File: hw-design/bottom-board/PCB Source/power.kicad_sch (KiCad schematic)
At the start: 29 parts, among them J1 Power Jack, J2 HMI_POWER, U1 TL750M10CKVURG3, U15 LM2596S-5, U2 LD1117S50TR

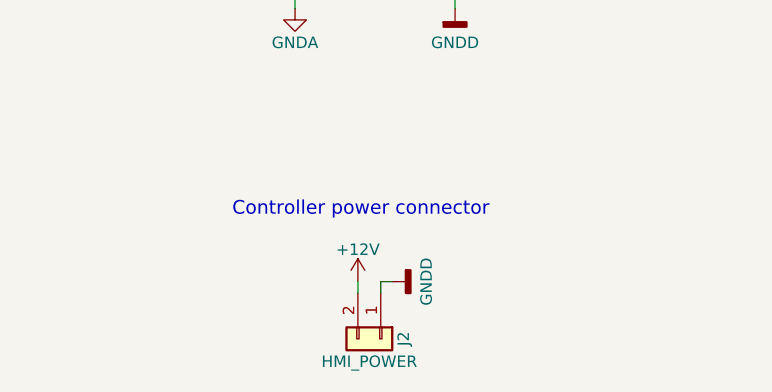
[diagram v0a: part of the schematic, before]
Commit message: change HMI connector type
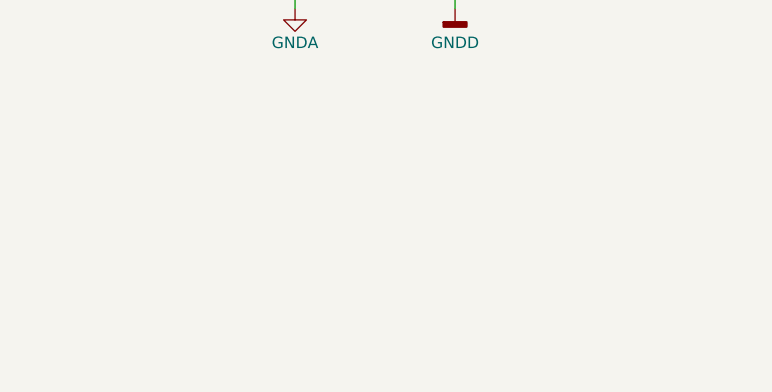
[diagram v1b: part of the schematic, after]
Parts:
- removed J2: HMI_POWER, footprints:B2B-XH-A, symbol bottom-board-rescue:Conn_01x02-Connector_Generic
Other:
- note removed: "Controller power connector"
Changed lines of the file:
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@@
-    (stroke (width 0) (type default) (color 0 0 0 0))
-  )
-  (wire (pts (xy 239.903 148.463) (xy 239.903 147.193))
     (stroke (width 0) (type default) (color 0 0 0 0))
   )
@@
     (stroke (width 0) (type default) (color 0 0 0 0))
   )
-  (wire (pts (xy 239.903 147.193) (xy 241.173 147.193))
-    (stroke (width 0) (type default) (color 0 0 0 0))
-  )
   (wire (pts (xy 195.072 99.06) (xy 195.072 93.98))
     (stroke (width 0) (type default) (color 0 0 0 0))
@@
   )
   (wire (pts (xy 175.768 101.092) (xy 175.768 99.06))
-    (stroke (width 0) (type default) (color 0 0 0 0))
-  )
-  (wire (pts (xy 237.363 147.193) (xy 237.363 148.463))
     (stroke (width 0) (type default) (color 0 0 0 0))
   )
@@
   (text "Digital" (at 159.639 81.534 180)
     (effects (font (size 2.54 2.54)) (justify right bottom))
-  )
-  (text "Controller power connector" (at 223.393 140.081 0)
-    (effects (font (size 1.524 1.524)) (justify left bottom))
   )
   (text "Analog" (at 131.699 24.257 180)
@@
     )
     (pin "1")
-  )
-  (symbol (lib_id "bottom-board-rescue:Conn_01x02-Connector_Generic") (at 239.903 153.543 270) (unit 1)
-    (in_bom yes) (on_board yes)
-    (property "Reference" "J2" (id 0) (at 242.443 153.543 0))
-    (property "Value" "HMI_POWER" (id 1) (at 238.633 156.083 90))
-    (property "Footprint" "footprints:B2B-XH-A" (id 2) (at 239.903 153.543 0)
-      (effects (font (size 1.27 1.27)) hide)
-    )
-    (property "Datasheet" "" (id 3) (at 239.903 153.543 0)
-      (effects (font (size 1.27 1.27)) hide)
-    )
-    (property "MPN" "B2B-XH-A(LF)(SN)" (id 4) (at 180.213 109.093 0)
-      (effects (font (size 1.27 1.27)) hide)
-    )
-    (pin "1")
-    (pin "2")
-  )
-  (symbol (lib_id "bottom-board-rescue:GNDD-power") (at 241.173 147.193 90) (mirror x) (unit 1)
-    (in_bom yes) (on_board yes)
-    (property "Reference" "#PWR029" (id 0) (at 247.523 147.193 0)
-      (effects (font (size 1.27 1.27)) hide)
-    )
-    (property "Value" "GNDD" (id 1) (at 244.983 147.193 0))
-    (property "Footprint" "" (id 2) (at 241.173 147.193 0)
-      (effects (font (size 1.524 1.524)))
-    )
-    (property "Datasheet" "" (id 3) (at 241.173 147.193 0)
-      (effects (font (size 1.524 1.524)))
-    )
-    (pin "1")
-  )
-  (symbol (lib_id "bottom-board-rescue:+12V-power") (at 237.363 147.193 0) (unit 1)
-    (in_bom yes) (on_board yes)
-    (property "Reference" "#PWR030" (id 0) (at 237.363 151.003 0)
-      (effects (font (size 1.27 1.27)) hide)
-    )
-    (property "Value" "+12V" (id 1) (at 237.363 143.637 0))
-    (property "Footprint" "" (id 2) (at 237.363 147.193 0)
-      (effects (font (size 1.524 1.524)))
-    )
-    (property "Datasheet" "" (id 3) (at 237.363 147.193 0)
-      (effects (font (size 1.524 1.524)))
-    )
-    (pin "1")

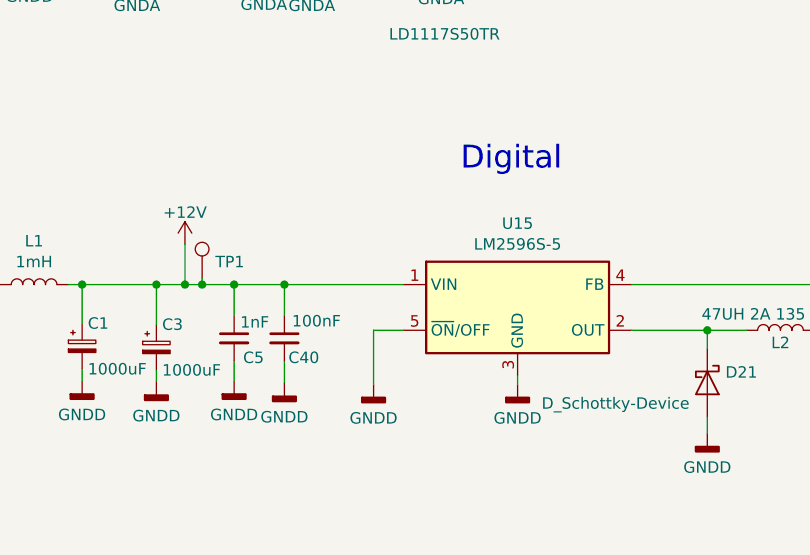
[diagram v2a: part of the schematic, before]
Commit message: mainboard: correct CC TX pin + update fabrication files
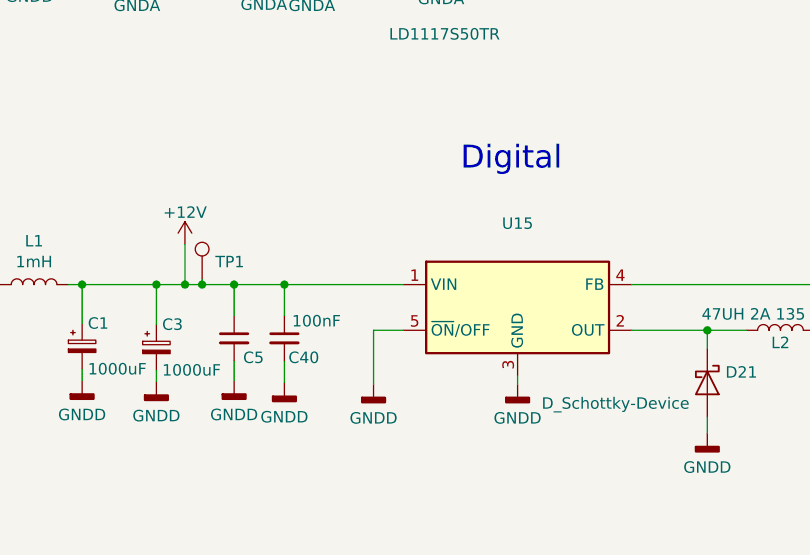
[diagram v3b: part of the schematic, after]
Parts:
- C5: value 1nF -> (none); footprint Capacitor_SMD:C_0603_1608Metric -> (none); MPN C0603X7R500-103KNP -> C0603X7R500-102KNP
- U15: value LM2596S-5 -> (none); footprint Package_TO_SOT_SMD:TO-263-5_TabPin3 -> (none); MPN2 (none) -> LM2596S-5
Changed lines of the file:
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@@
     (in_bom yes) (on_board yes)
     (property "Reference" "C5" (id 0) (at 125.349 102.108 0))
-    (property "Value" "1nF" (id 1) (at 125.476 98.171 0))
-    (property "Footprint" "Capacitor_SMD:C_0603_1608Metric" (id 2) (at 123.19 99.949 0)
+    (property "Value" "" (id 1) (at 125.476 98.171 0))
+    (property "Footprint" "" (id 2) (at 123.19 99.949 0)
       (effects (font (size 1.524 1.524)) hide)
     )
@@
       (effects (font (size 1.524 1.524)))
     )
-    (property "MPN" "C0603X7R500-103KNP" (id 4) (at -11.43 235.839 0)
+    (property "MPN" "C0603X7R500-102KNP" (id 4) (at -11.43 235.839 0)
       (effects (font (size 1.27 1.27)) hide)
     )
@@
     (in_bom yes) (on_board yes)
     (property "Reference" "U15" (id 0) (at 154.686 87.1982 0))
-    (property "Value" "LM2596S-5" (id 1) (at 154.686 89.5096 0))
-    (property "Footprint" "Package_TO_SOT_SMD:TO-263-5_TabPin3" (id 2) (at 155.956 102.87 0)
+    (property "Value" "" (id 1) (at 154.686 89.5096 0))
+    (property "Footprint" "" (id 2) (at 155.956 102.87 0)
       (effects (font (size 1.27 1.27) italic) (justify left) hide)
     )
@@
       (effects (font (size 1.27 1.27)) hide)
     )
+    (property "MPN2" "LM2596S-5" (id 5) (at 154.686 96.52 0)
+      (effects (font (size 1.524 1.524)) hide)
+    )
     (pin "1")
